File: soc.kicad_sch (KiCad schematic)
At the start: 89 parts, among them U1 MPFS250T-FCVG484

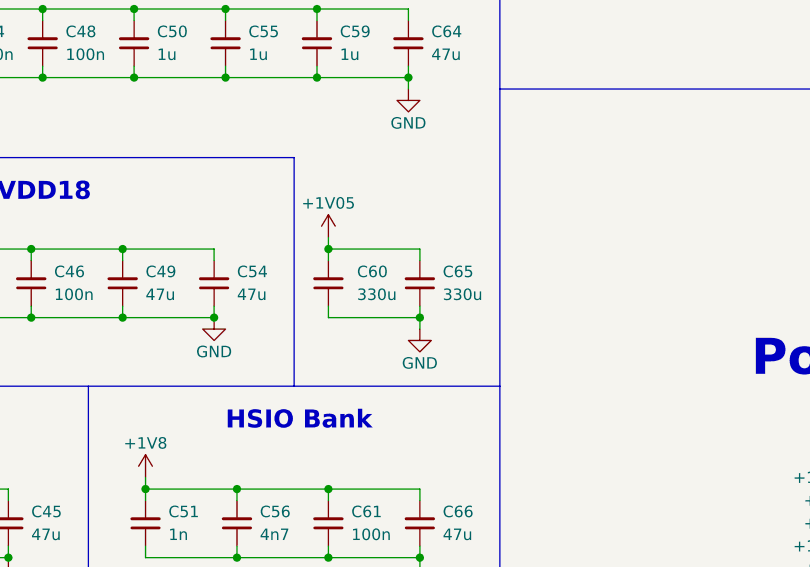
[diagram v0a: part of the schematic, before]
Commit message: [#54899] Replace 330u capacitors
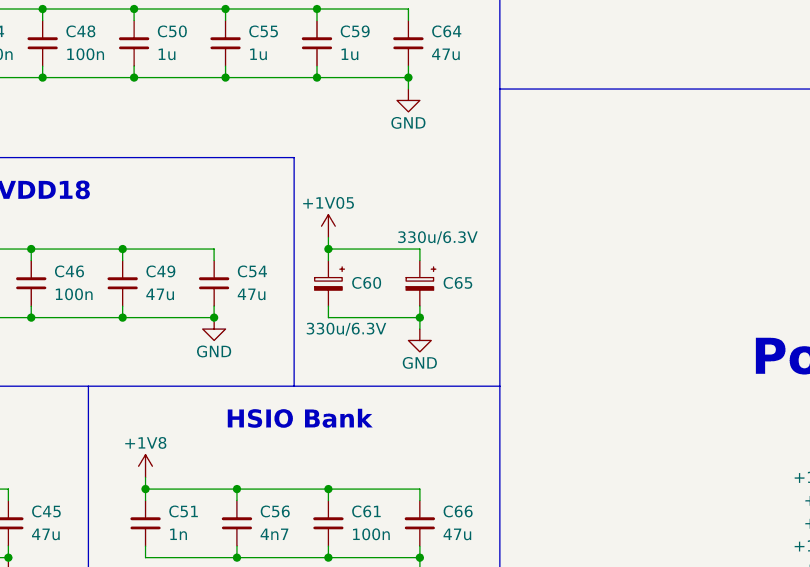
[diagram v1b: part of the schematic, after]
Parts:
- removed C60, C65: C_330u_1210, antmicro-footprints:C_1210_3225Metric, symbol antmicroCapacitorsmisc:C_330u_1210
- added C60, C65: C_Pol_330u_6.3V_KEMET-T520-B, antmicro-footprints:C_Pol_EIA-B, symbol antmicroCapacitorspol:C_Pol_330u_6.3V_KEMET-T520-B
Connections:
- net +1V05: now also C60.1, C65.1
- net GND: now also C60.2, C65.2
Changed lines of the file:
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@@
     )
   )
+  (symbol (lib_id "antmicroCapacitorspol:C_Pol_330u_6.3V_KEMET-T520-B") (at 172.72 190.5 270) (unit 1)
+    (in_bom yes) (on_board yes) (dnp no)
+    (property "Reference" "C60" (at 175.26 193.04 90)
+      (effects (font (size 1.27 1.27) (thickness 0.15)) (justify left))
+    )
+    (property "Value" "C_Pol_330u_6.3V_KEMET-T520-B" (at 170.18 204.47 0)
+      (effects (font (size 1.27 1.27) (thickness 0.15)) (justify left bottom) hide)
+    )
+    (property "Footprint" "antmicro-footprints:C_Pol_EIA-B" (at 165.1 204.47 0)
+      (effects (font (size 1.27 1.27) (thickness 0.15)) (justify left bottom) hide)
+    )
+    (property "Datasheet" "https://content.kemet.com/datasheets/KEM_T2076_T52X-530.pdf" (at 162.56 204.47 0)
+      (effects (font (size 1.27 1.27) (thickness 0.15)) (justify left bottom) hide)
+    )
+    (property "Val" "330u/6.3V" (at 170.18 198.12 90)
+      (effects (font (size 1.27 1.27) (thickness 0.15)) (justify left))
+    )
+    (property "MPN" "T520B337M006ATE040" (at 160.02 204.47 0)
+      (effects (font (size 1.27 1.27) (thickness 0.15)) (justify left bottom) hide)
+    )
+    (property "Manufacturer" "KEMET" (at 157.48 204.47 0)
+      (effects (font (size 1.27 1.27) (thickness 0.15)) (justify left bottom) hide)
+    )
+    (property "License" "Apache-2.0" (at 154.94 204.47 0)
+      (effects (font (size 1.27 1.27) (thickness 0.15)) (justify left bottom) hide)
+    )
+    (property "Author" "Antmicro" (at 152.4 204.47 0)
+      (effects (font (size 1.27 1.27) (thickness 0.15)) (justify left bottom) hide)
+    )
+    (property "Voltage" "6.3V" (at 149.86 204.47 0)
+      (effects (font (size 1.27 1.27)) (justify left bottom) hide)
+    )
+    (property "Dielectric" "template_dielectric" (at 147.32 204.47 0)
+      (effects (font (size 1.27 1.27)) (justify left bottom) hide)
+    )
+    (pin "1")
+    (pin "2")
+    (instances
+      (project "polarfire-som"
+        (path "/db4a0d3e-2eb3-499e-977d-6eb378cfd3ed/99f116ae-bc8e-42a5-8f88-aecc401b3bcc"
+          (reference "C60") (unit 1)
+        )
+      )
+    )
+  )
   (symbol (lib_id "antmicroResistors0402:R_49R9_0402") (at 146.05 48.26 0) (mirror x) (unit 1)
     (in_bom yes) (on_board yes) (dnp no)
@@
     )
   )
-  (symbol (lib_id "antmicroCapacitorsmisc:C_330u_1210") (at 172.72 195.58 90) (unit 1)
-    (in_bom yes) (on_board yes) (dnp no) (fields_autoplaced)
-    (property "Reference" "C60" (at 175.895 191.7635 90)
-      (effects (font (size 1.27 1.27) (thickness 0.15)) (justify right))
-    )
-    (property "Value" "C_330u_1210" (at 182.88 175.26 0)
-      (effects (font (size 1.27 1.27) (thickness 0.15)) (justify left bottom) hide)
-    )
-    (property "Footprint" "antmicro-footprints:C_1210_3225Metric" (at 185.42 175.26 0)
-      (effects (font (size 1.27 1.27) (thickness 0.15)) (justify left bottom) hide)
-    )
-    (property "Datasheet" "https://www.mouser.pl/datasheet/2/40/TCJ-2887130.pdf" (at 187.96 175.26 0)
-      (effects (font (size 1.27 1.27) (thickness 0.15)) (justify left bottom) hide)
-    )
-    (property "MPN" "TCJB337M002R0045E " (at 190.5 175.26 0)
-      (effects (font (size 1.27 1.27) (thickness 0.15)) (justify left bottom) hide)
-    )
-    (property "Manufacturer" "KYOCERA AVX " (at 193.04 175.26 0)
-      (effects (font (size 1.27 1.27) (thickness 0.15)) (justify left bottom) hide)
-    )
-    (property "License" "Apache-2.0" (at 195.58 175.26 0)
-      (effects (font (size 1.27 1.27) (thickness 0.15)) (justify left bottom) hide)
-    )
-    (property "Author" "Antmicro" (at 198.12 175.26 0)
-      (effects (font (size 1.27 1.27) (thickness 0.15)) (justify left bottom) hide)
-    )
-    (property "Val" "330u" (at 175.895 194.3035 90)
-      (effects (font (size 1.27 1.27) (thickness 0.15)) (justify right))
-    )
-    (property "Voltage" "" (at 200.66 175.26 0)
-      (effects (font (size 1.27 1.27)) (justify left bottom) hide)
-    )
-    (property "Dielectric" "" (at 203.2 175.26 0)
-      (effects (font (size 1.27 1.27)) (justify left bottom) hide)
-    )
-    (pin "1")
-    (pin "2")
-    (instances
-      (project "polarfire-som"
-        (path "/db4a0d3e-2eb3-499e-977d-6eb378cfd3ed/99f116ae-bc8e-42a5-8f88-aecc401b3bcc"
-          (reference "C60") (unit 1)
-        )
-      )
-    )
-  )
   (symbol (lib_id "antmicroCapacitors0402:C_10n_0402") (at 162.56 275.59 90) (unit 1)
     (in_bom yes) (on_board yes) (dnp no) (fields_autoplaced)
@@
     )
   )
-  (symbol (lib_id "antmicroCapacitorsmisc:C_330u_1210") (at 182.88 195.58 90) (unit 1)
-    (in_bom yes) (on_board yes) (dnp no) (fields_autoplaced)
-    (property "Reference" "C65" (at 185.42 191.7635 90)
-      (effects (font (size 1.27 1.27) (thickness 0.15)) (justify right))
-    )
-    (property "Value" "C_330u_1210" (at 193.04 175.26 0)
-      (effects (font (size 1.27 1.27) (thickness 0.15)) (justify left bottom) hide)
-    )
-    (property "Footprint" "antmicro-footprints:C_1210_3225Metric" (at 195.58 175.26 0)
-      (effects (font (size 1.27 1.27) (thickness 0.15)) (justify left bottom) hide)
-    )
-    (property "Datasheet" "https://www.mouser.pl/datasheet/2/40/TCJ-2887130.pdf" (at 198.12 175.26 0)
-      (effects (font (size 1.27 1.27) (thickness 0.15)) (justify left bottom) hide)
-    )
-    (property "MPN" "TCJB337M002R0045E " (at 200.66 175.26 0)
-      (effects (font (size 1.27 1.27) (thickness 0.15)) (justify left bottom) hide)
-    )
-    (property "Manufacturer" "KYOCERA AVX " (at 203.2 175.26 0)
-      (effects (font (size 1.27 1.27) (thickness 0.15)) (justify left bottom) hide)
-    )
-    (property "License" "Apache-2.0" (at 205.74 175.26 0)
-      (effects (font (size 1.27 1.27) (thickness 0.15)) (justify left bottom) hide)
-    )
-    (property "Author" "Antmicro" (at 208.28 175.26 0)
-      (effects (font (size 1.27 1.27) (thickness 0.15)) (justify left bottom) hide)
-    )
-    (property "Val" "330u" (at 185.42 194.3035 90)
-      (effects (font (size 1.27 1.27) (thickness 0.15)) (justify right))
-    )
-    (property "Voltage" "" (at 210.82 175.26 0)
-      (effects (font (size 1.27 1.27)) (justify left bottom) hide)
-    )
-    (property "Dielectric" "" (at 213.36 175.26 0)
-      (effects (font (size 1.27 1.27)) (justify left bottom) hide)
-    )
-    (pin "1")
-    (pin "2")
-    (instances
-      (project "polarfire-som"
-        (path "/db4a0d3e-2eb3-499e-977d-6eb378cfd3ed/99f116ae-bc8e-42a5-8f88-aecc401b3bcc"
-          (reference "C65") (unit 1)
-        )
-      )
-    )
-  )
   (symbol (lib_id "antmicroCapacitorsmisc:C_100n_0201_25V") (at 116.84 222.25 90) (unit 1)
     (in_bom yes) (on_board yes) (dnp no) (fields_autoplaced)
@@
         )
       )
+    )
+  )
+  (symbol (lib_id "antmicroCapacitorspol:C_Pol_330u_6.3V_KEMET-T520-B") (at 182.88 190.5 270) (unit 1)
+    (in_bom yes) (on_board yes) (dnp no)
+    (property "Reference" "C65" (at 185.42 193.04 90)
+      (effects (font (size 1.27 1.27) (thickness 0.15)) (justify left))
+    )
+    (property "Value" "C_Pol_330u_6.3V_KEMET-T520-B" (at 180.34 204.47 0)
+      (effects (font (size 1.27 1.27) (thickness 0.15)) (justify left bottom) hide)
+    )
+    (property "Footprint" "antmicro-footprints:C_Pol_EIA-B" (at 175.26 204.47 0)
+      (effects (font (size 1.27 1.27) (thickness 0.15)) (justify left bottom) hide)
+    )
+    (property "Datasheet" "https://content.kemet.com/datasheets/KEM_T2076_T52X-530.pdf" (at 172.72 204.47 0)
+      (effects (font (size 1.27 1.27) (thickness 0.15)) (justify left bottom) hide)
+    )
+    (property "Val" "330u/6.3V" (at 180.34 187.96 90)
+      (effects (font (size 1.27 1.27) (thickness 0.15)) (justify left))
+    )
+    (property "MPN" "T520B337M006ATE040" (at 170.18 204.47 0)
+      (effects (font (size 1.27 1.27) (thickness 0.15)) (justify left bottom) hide)
+    )
+    (property "Manufacturer" "KEMET" (at 167.64 204.47 0)
+      (effects (font (size 1.27 1.27) (thickness 0.15)) (justify left bottom) hide)
+    )
+    (property "License" "Apache-2.0" (at 165.1 204.47 0)
+      (effects (font (size 1.27 1.27) (thickness 0.15)) (justify left bottom) hide)
+    )
+    (property "Author" "Antmicro" (at 162.56 204.47 0)
+      (effects (font (size 1.27 1.27) (thickness 0.15)) (justify left bottom) hide)
+    )
+    (property "Voltage" "6.3V" (at 160.02 204.47 0)
+      (effects (font (size 1.27 1.27)) (justify left bottom) hide)
+    )
+    (property "Dielectric" "template_dielectric" (at 157.48 204.47 0)
+      (effects (font (size 1.27 1.27)) (justify left bottom) hide)
+    )
+    (pin "1")
+    (pin "2")
+    (instances
+      (project "polarfire-som"
+        (path "/db4a0d3e-2eb3-499e-977d-6eb378cfd3ed/99f116ae-bc8e-42a5-8f88-aecc401b3bcc"
+          (reference "C65") (unit 1)
+        )
+      )

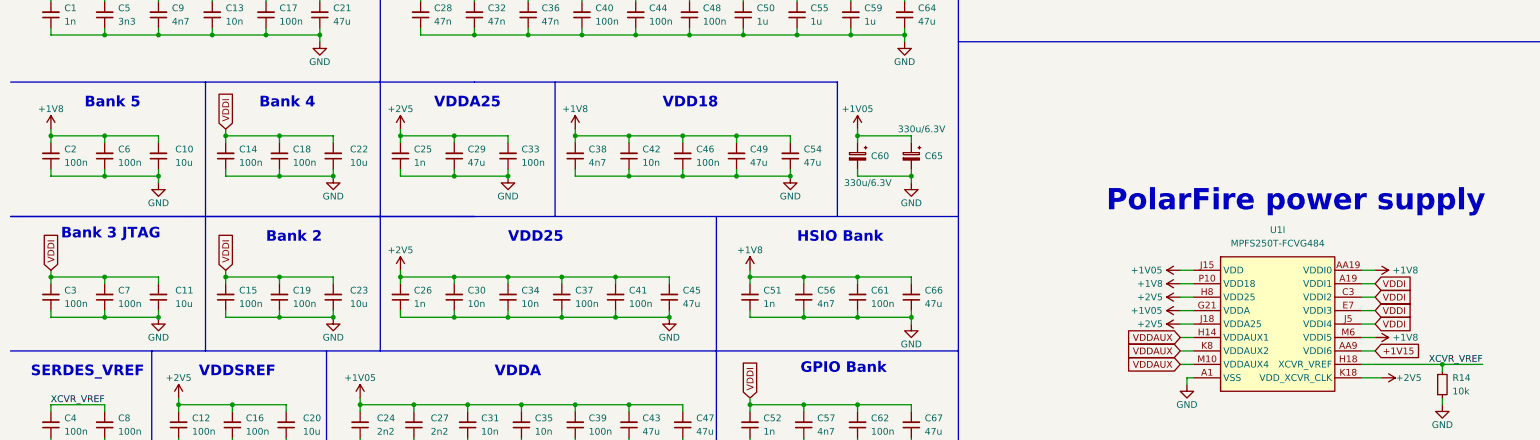
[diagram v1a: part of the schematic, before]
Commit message: [#54899] Change PF Bank 5 supply to 3V3
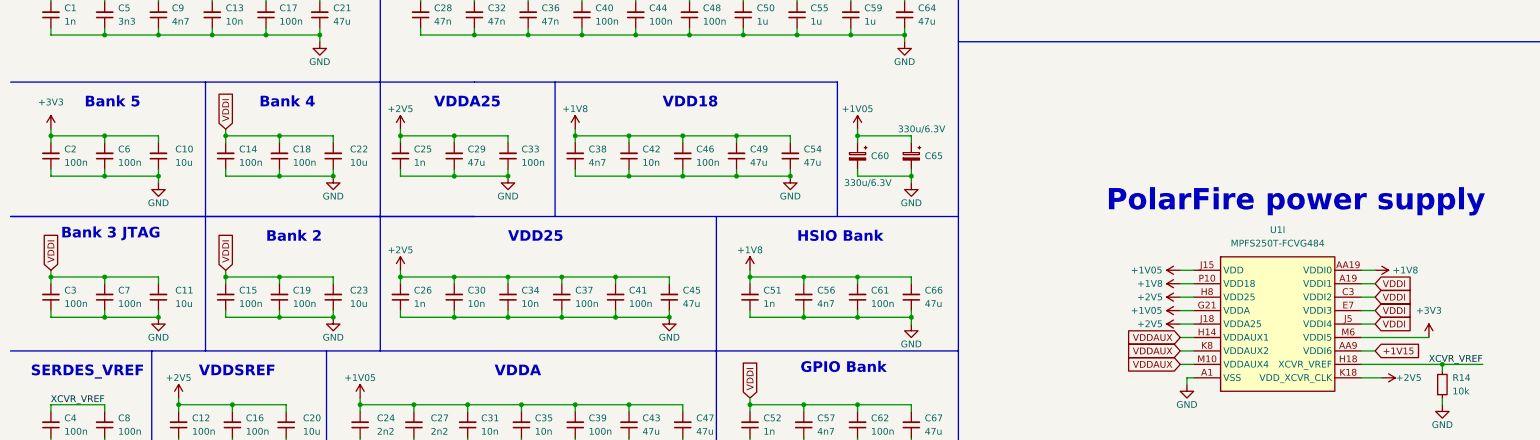
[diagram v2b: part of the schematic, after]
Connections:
- net +1V8: no longer C10.2, C2.2, C6.2, U1.M6 (VDDI5), U1.M8 (VDDI5)
- net +3V3: now also C10.2, C2.2, C6.2, U1.M6 (VDDI5), U1.M8 (VDDI5)
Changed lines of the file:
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@@
     (stroke (width 0) (type default))
   )
-  (wire (pts (xy 267.97 227.33) (xy 270.51 227.33))
+  (wire (pts (xy 267.97 227.33) (xy 280.67 227.33))
     (stroke (width 0) (type default))
   )
@@
     )
   )
-  (symbol (lib_id "antmicropower:+1V8") (at 20.32 187.96 0) (unit 1)
-    (in_bom yes) (on_board yes) (dnp no)
-    (property "Reference" "#PWR010" (at 35.56 190.5 0)
-      (effects (font (size 1.27 1.27) (thickness 0.15)) (justify left bottom) hide)
-    )
-    (property "Value" "+1V8" (at 20.32 184.15 0)
-      (effects (font (size 1.27 1.27) (thickness 0.15)))
-    )
-    (property "Footprint" "" (at 35.56 195.58 0)
-      (effects (font (size 1.27 1.27) (thickness 0.15)) (justify left bottom) hide)
-    )
-    (property "Datasheet" "" (at 35.56 198.12 0)
-      (effects (font (size 1.27 1.27) (thickness 0.15)) (justify left bottom) hide)
-    )
-    (property "Author" "Antmicro" (at 35.56 195.58 0)
-      (effects (font (size 1.27 1.27) (thickness 0.15)) (justify left bottom) hide)
-    )
-    (property "License" "Apache-2.0" (at 35.56 198.12 0)
-      (effects (font (size 1.27 1.27) (thickness 0.15)) (justify left bottom) hide)
-    )
-    (pin "1")
-    (instances
-      (project "polarfire-som"
-        (path "/db4a0d3e-2eb3-499e-977d-6eb378cfd3ed/99f116ae-bc8e-42a5-8f88-aecc401b3bcc"
-          (reference "#PWR010") (unit 1)
-        )
-      )
-    )
-  )
   (symbol (lib_id "antmicroCapacitorsmisc:C_100n_0201_25V") (at 30.48 222.25 90) (unit 1)
     (in_bom yes) (on_board yes) (dnp no) (fields_autoplaced)
@@
     )
   )
+  (symbol (lib_name "+3V3_2") (lib_id "antmicropower:+3V3") (at 20.32 187.96 0) (unit 1)
+    (in_bom yes) (on_board yes) (dnp no) (fields_autoplaced)
+    (property "Reference" "#PWR010" (at 35.56 187.96 0)
+      (effects (font (size 1.27 1.27) (thickness 0.15)) (justify left bottom) hide)
+    )
+    (property "Value" "+3V3" (at 20.32 182.88 0)
+      (effects (font (size 1.27 1.27) (thickness 0.15)))
+    )
+    (property "Footprint" "" (at 35.56 195.58 0)
+      (effects (font (size 1.27 1.27) (thickness 0.15)) (justify left bottom) hide)
+    )
+    (property "Datasheet" "" (at 35.56 198.12 0)
+      (effects (font (size 1.27 1.27) (thickness 0.15)) (justify left bottom) hide)
+    )
+    (property "Author" "Antmicro" (at 35.56 190.5 0)
+      (effects (font (size 1.27 1.27) (thickness 0.15)) (justify left bottom) hide)
+    )
+    (property "License" "Apache-2.0" (at 35.56 193.04 0)
+      (effects (font (size 1.27 1.27) (thickness 0.15)) (justify left bottom) hide)
+    )
+    (pin "1")
+    (instances
+      (project "polarfire-som"
+        (path "/db4a0d3e-2eb3-499e-977d-6eb378cfd3ed/99f116ae-bc8e-42a5-8f88-aecc401b3bcc"
+          (reference "#PWR010") (unit 1)
+        )
+      )
+    )
+  )
   (symbol (lib_id "antmicroResistors0402:R_100R_0402") (at 370.84 226.06 90) (unit 1)
     (in_bom no) (on_board yes) (dnp no)
@@
     )
   )
+  (symbol (lib_name "+3V3_1") (lib_id "antmicropower:+3V3") (at 280.67 227.33 0) (unit 1)
+    (in_bom yes) (on_board yes) (dnp no) (fields_autoplaced)
+    (property "Reference" "#PWR042" (at 295.91 227.33 0)
+      (effects (font (size 1.27 1.27) (thickness 0.15)) (justify left bottom) hide)
+    )
+    (property "Value" "+3V3" (at 280.67 222.25 0)
+      (effects (font (size 1.27 1.27) (thickness 0.15)))
+    )
+    (property "Footprint" "" (at 295.91 234.95 0)
+      (effects (font (size 1.27 1.27) (thickness 0.15)) (justify left bottom) hide)
+    )
+    (property "Datasheet" "" (at 295.91 237.49 0)
+      (effects (font (size 1.27 1.27) (thickness 0.15)) (justify left bottom) hide)
+    )
+    (property "Author" "Antmicro" (at 295.91 229.87 0)
+      (effects (font (size 1.27 1.27) (thickness 0.15)) (justify left bottom) hide)
+    )
+    (property "License" "Apache-2.0" (at 295.91 232.41 0)
+      (effects (font (size 1.27 1.27) (thickness 0.15)) (justify left bottom) hide)
+    )
+    (pin "1")
+    (instances
+      (project "polarfire-som"
+        (path "/db4a0d3e-2eb3-499e-977d-6eb378cfd3ed/99f116ae-bc8e-42a5-8f88-aecc401b3bcc"
+          (reference "#PWR042") (unit 1)
+        )
+      )
+    )
+  )
   (symbol (lib_id "antmicroCapacitors0603:C_47u_0603") (at 129.54 246.38 90) (unit 1)
     (in_bom yes) (on_board yes) (dnp no) (fields_autoplaced)
@@
         )
       )
-    )
-  )
-  (symbol (lib_id "antmicropower:+1V8") (at 270.51 227.33 270) (unit 1)
-    (in_bom yes) (on_board yes) (dnp no)
-    (property "Reference" "#PWR042" (at 267.97 242.57 0)
-      (effects (font (size 1.27 1.27) (thickness 0.15)) (justify left bottom) hide)
-    )
-    (property "Value" "+1V8" (at 276.225 227.33 90)
-      (effects (font (size 1.27 1.27) (thickness 0.15)))
-    )
-    (property "Footprint" "" (at 262.89 242.57 0)
-      (effects (font (size 1.27 1.27) (thickness 0.15)) (justify left bottom) hide)
-    )
-    (property "Datasheet" "" (at 260.35 242.57 0)
-      (effects (font (size 1.27 1.27) (thickness 0.15)) (justify left bottom) hide)
-    )
-    (property "Author" "Antmicro" (at 262.89 242.57 0)
-      (effects (font (size 1.27 1.27) (thickness 0.15)) (justify left bottom) hide)
-    )
-    (property "License" "Apache-2.0" (at 260.35 242.57 0)
-      (effects (font (size 1.27 1.27) (thickness 0.15)) (justify left bottom) hide)
-    )
-    (pin "1")
-    (instances
-      (project "polarfire-som"
-        (path "/db4a0d3e-2eb3-499e-977d-6eb378cfd3ed/99f116ae-bc8e-42a5-8f88-aecc401b3bcc"
-          (reference "#PWR042") (unit 1)
-        )
-      )
